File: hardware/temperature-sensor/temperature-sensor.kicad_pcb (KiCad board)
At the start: 2 copper layers, 56 x 56 mm, 3 parts, among them J1 1881626, U1 STM32F407V_E-G_Tx, U2 LAN8720A

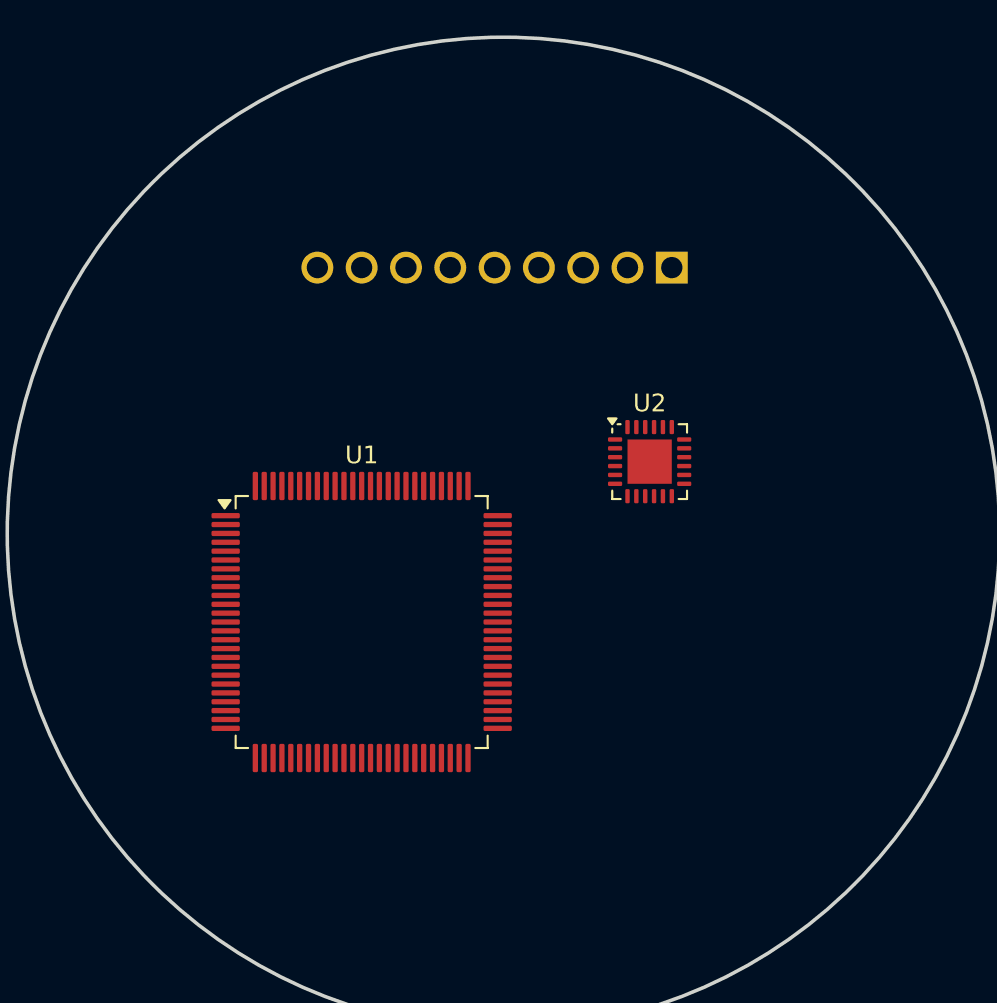
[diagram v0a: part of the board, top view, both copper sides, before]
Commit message: add components for temperature sensor
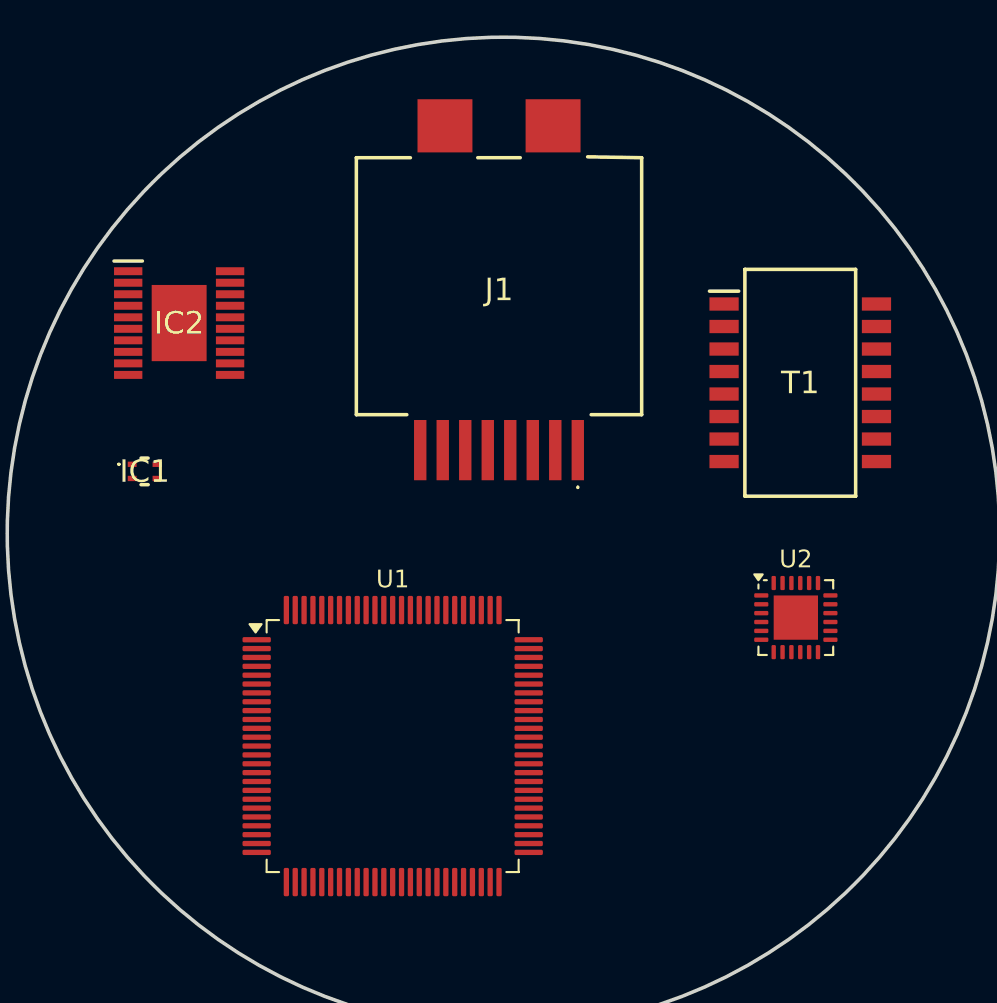
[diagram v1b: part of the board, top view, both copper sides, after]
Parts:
- added IC1: SHT40-CD1B-R3, benediktibk:SHT40CD1BR3, F.Cu at (129.8, 95.5)
- added IC2: PM8803TR, benediktibk:SOP65P640X120-21N, F.Cu at (131.7, 87.1)
- added T1: PT61018PEL, benediktibk:SOIC127P930X565-16N, F.Cu at (166.8, 90.5)
- J1: value 1881626 -> 1149611; footprint benediktibk:phoenix_contact_1881626 -> benediktibk:1149611; moved to F.Cu
- moved U2 12.1 mm to (166.5, 103.8)
- moved J1 9.83 mm to (149.8, 85.2), turned to 0 degrees
- moved U1 7.22 mm to (143.8, 111.0)

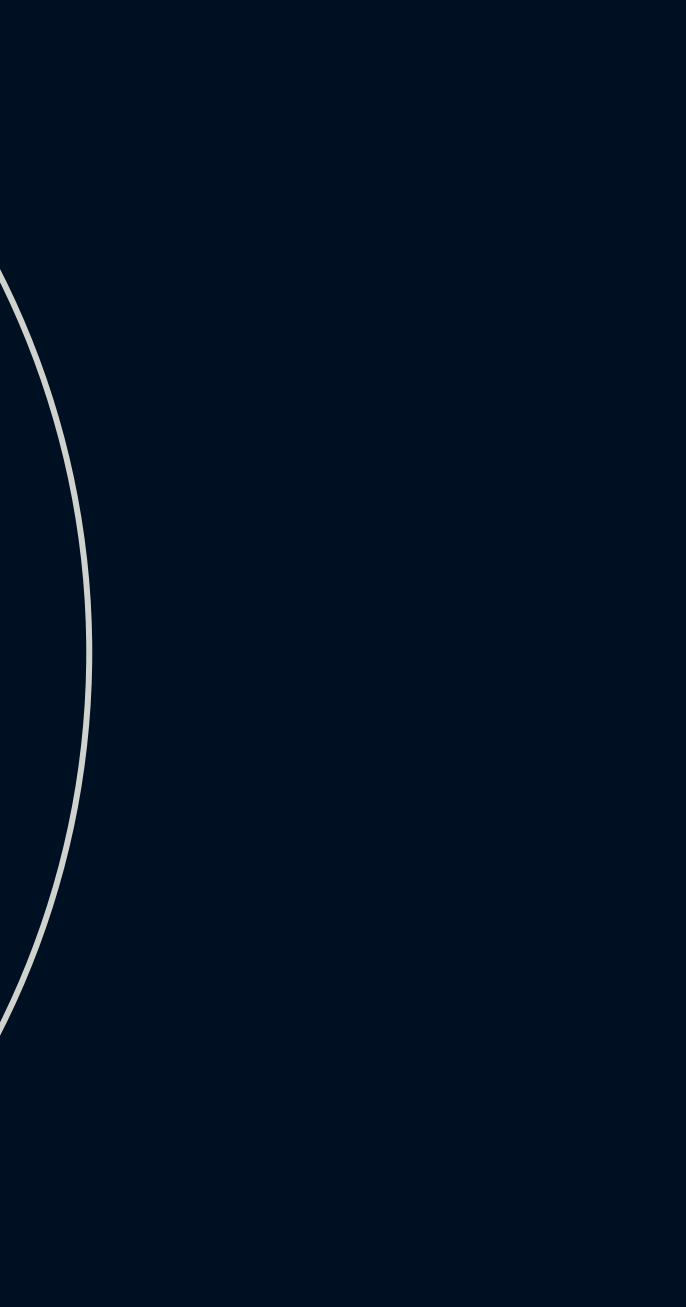
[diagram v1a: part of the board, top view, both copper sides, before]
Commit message: extend schematic of ethernet
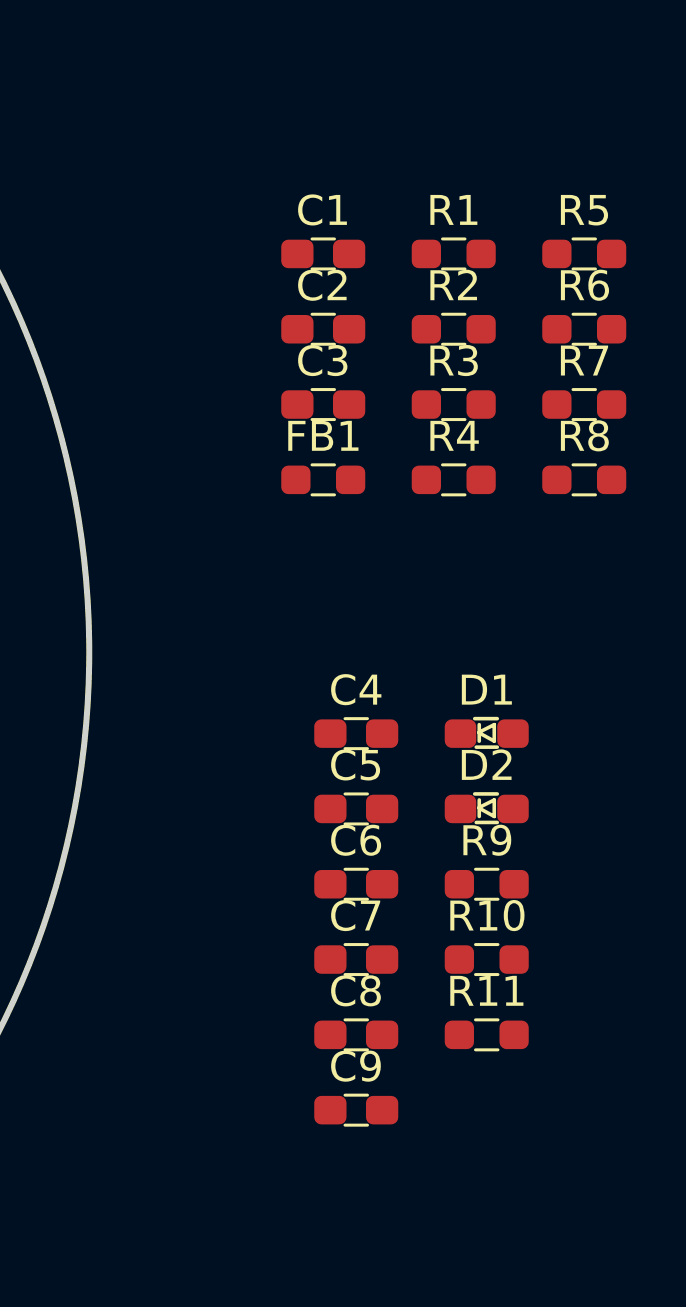
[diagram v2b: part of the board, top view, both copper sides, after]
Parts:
- added C1: 1nF 1kV, benediktibk:C_0603_1608Metric_Pad1.08x0.95mm_HandSolder, F.Cu at (185.8, 85.7)
- added C2: 100nF, benediktibk:C_0603_1608Metric_Pad1.08x0.95mm_HandSolder, F.Cu at (185.8, 88.2)
- added C3: 100nF, benediktibk:C_0603_1608Metric_Pad1.08x0.95mm_HandSolder, F.Cu at (185.8, 90.7)
- added C4: 100nF, benediktibk:C_0603_1608Metric_Pad1.08x0.95mm_HandSolder, F.Cu at (186.9, 101.7)
- added C5: 100nF, benediktibk:C_0603_1608Metric_Pad1.08x0.95mm_HandSolder, F.Cu at (186.9, 104.2)
- added C6: 100nF, benediktibk:C_0603_1608Metric_Pad1.08x0.95mm_HandSolder, F.Cu at (186.9, 106.7)
- added C7: 1uF, benediktibk:C_0603_1608Metric_Pad1.08x0.95mm_HandSolder, F.Cu at (186.9, 109.2)
- added C8: 1uF, benediktibk:C_0603_1608Metric_Pad1.08x0.95mm_HandSolder, F.Cu at (186.9, 111.8)
- added C9: 470pF, benediktibk:C_0603_1608Metric_Pad1.08x0.95mm_HandSolder, F.Cu at (186.9, 114.3)
- added D1: link/active, benediktibk:D_0603_1608Metric_Pad1.05x0.95mm_HandSolder, F.Cu at (191.2, 101.7)
- added D2: 100Mbps, benediktibk:D_0603_1608Metric_Pad1.05x0.95mm_HandSolder, F.Cu at (191.2, 104.2)
- added FB1: BLM18P, benediktibk:R_0603_1608Metric_Pad0.98x0.95mm_HandSolder, F.Cu at (185.8, 93.2)
- added R1: 75Ohm, benediktibk:R_0603_1608Metric_Pad0.98x0.95mm_HandSolder, F.Cu at (190.2, 85.7)
- added R10: 270Ohm, benediktibk:R_0603_1608Metric_Pad0.98x0.95mm_HandSolder, F.Cu at (191.2, 109.2)
- added R11: 12.1kOhm, benediktibk:R_0603_1608Metric_Pad0.98x0.95mm_HandSolder, F.Cu at (191.2, 111.8)
- added R2: 75Ohm, benediktibk:R_0603_1608Metric_Pad0.98x0.95mm_HandSolder, F.Cu at (190.2, 88.2)
- added R3: 75Ohm, benediktibk:R_0603_1608Metric_Pad0.98x0.95mm_HandSolder, F.Cu at (190.2, 90.7)
- added R4: 75Ohm, benediktibk:R_0603_1608Metric_Pad0.98x0.95mm_HandSolder, F.Cu at (190.2, 93.2)
- added R5: 47Ohm, benediktibk:R_0603_1608Metric_Pad0.98x0.95mm_HandSolder, F.Cu at (194.5, 85.7)
- added R6: 47Ohm, benediktibk:R_0603_1608Metric_Pad0.98x0.95mm_HandSolder, F.Cu at (194.5, 88.2)
- added R7: 47Ohm, benediktibk:R_0603_1608Metric_Pad0.98x0.95mm_HandSolder, F.Cu at (194.5, 90.7)
- added R8: 47Ohm, benediktibk:R_0603_1608Metric_Pad0.98x0.95mm_HandSolder, F.Cu at (194.5, 93.2)
- added R9: 270Ohm, benediktibk:R_0603_1608Metric_Pad0.98x0.95mm_HandSolder, F.Cu at (191.2, 106.7)
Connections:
- J1 pad 1: unconnected-(J1-Pad1) -> Net-(T1-TX+)
- J1 pad 2: unconnected-(J1-Pad2) -> Net-(T1-TX-)
- J1 pad 3: unconnected-(J1-Pad3) -> Net-(T1-RX+)
- J1 pad 4: unconnected-(J1-Pad4) -> Net-(J1-Pad4)
- J1 pad 5: unconnected-(J1-Pad5) -> Net-(J1-Pad4)
- J1 pad 6: unconnected-(J1-Pad6) -> Net-(T1-RX-)
- J1 pad 7: unconnected-(J1-Pad7) -> Net-(J1-Pad7)
- J1 pad 8: unconnected-(J1-Pad8) -> Net-(J1-Pad7)
- J1 pad MP1: unconnected-(J1-PadMP1) -> GND
- J1 pad MP2: unconnected-(J1-PadMP2) -> GND
- T1 pad 1: unconnected-(T1-TD+-Pad1) -> /Ethernet/TX_P
- T1 pad 10: unconnected-(T1-CT_3-Pad10) -> Net-(T1-CT_3)
- T1 pad 11: unconnected-(T1-RX+-Pad11) -> Net-(T1-RX+)
- T1 pad 14: unconnected-(T1-TX--Pad14) -> Net-(T1-TX-)
- T1 pad 15: unconnected-(T1-CT_4-Pad15) -> Net-(T1-CT_4)
- T1 pad 16: unconnected-(T1-TX+-Pad16) -> Net-(T1-TX+)
- T1 pad 2: unconnected-(T1-CT_1-Pad2) -> Net-(T1-CT_1)
- T1 pad 3: unconnected-(T1-TD--Pad3) -> /Ethernet/TX_N
- T1 pad 6: unconnected-(T1-RD+-Pad6) -> /Ethernet/RX_P
- T1 pad 7: unconnected-(T1-CT_2-Pad7) -> Net-(T1-CT_2)
- T1 pad 8: unconnected-(T1-RD--Pad8) -> /Ethernet/RX_N
- T1 pad 9: unconnected-(T1-RX--Pad9) -> Net-(T1-RX-)
- U2 pad 1: unconnected-(U2-VDD2A-Pad1) -> Net-(U2-VDD1A)
- U2 pad 10: unconnected-(U2-RXER/PHYAD0-Pad10) -> /Ethernet/RXER/PHYAD0
- U2 pad 11: unconnected-(U2-CRS_DV/MODE2-Pad11) -> /Ethernet/CRS_DV/MODE2
- U2 pad 12: unconnected-(U2-MDIO-Pad12) -> /Ethernet/MDIO
- U2 pad 13: unconnected-(U2-MDC-Pad13) -> /Ethernet/MDC
- U2 pad 14: unconnected-(U2-~{INT}/REFCLKO-Pad14) -> /Ethernet/REFCLK
- U2 pad 15: unconnected-(U2-~{RST}-Pad15) -> /Ethernet/nRST
- U2 pad 16: unconnected-(U2-TXEN-Pad16) -> /Ethernet/TXEN
- U2 pad 17: unconnected-(U2-TXD0-Pad17) -> /Ethernet/TXD0
- U2 pad 18: unconnected-(U2-TXD1-Pad18) -> /Ethernet/TXD1
- U2 pad 19: unconnected-(U2-VDD1A-Pad19) -> Net-(U2-VDD1A)
- U2 pad 2: unconnected-(U2-LED2/~{INTSEL}-Pad2) -> Net-(D2-A)
- U2 pad 20: unconnected-(U2-TXN-Pad20) -> /Ethernet/TX_N
- U2 pad 21: unconnected-(U2-TXP-Pad21) -> /Ethernet/TX_P
- U2 pad 22: unconnected-(U2-RXN-Pad22) -> /Ethernet/RX_N
- U2 pad 23: unconnected-(U2-RXP-Pad23) -> /Ethernet/RX_P
- U2 pad 24: unconnected-(U2-RBIAS-Pad24) -> Net-(U2-RBIAS)
- U2 pad 25: unconnected-(U2-VSS-Pad25) -> GND
- U2 pad 3: unconnected-(U2-LED1/REGOFF-Pad3) -> Net-(D1-A)
- U2 pad 6: unconnected-(U2-VDDCR-Pad6) -> Net-(U2-VDDCR)
- U2 pad 7: unconnected-(U2-RXD1/MODE1-Pad7) -> /Ethernet/RXD1/MODE1
- U2 pad 8: unconnected-(U2-RXD0/MODE0-Pad8) -> /Ethernet/RXD0/MODE0
- U2 pad 9: unconnected-(U2-VDDIO-Pad9) -> Net-(U2-VDD1A)

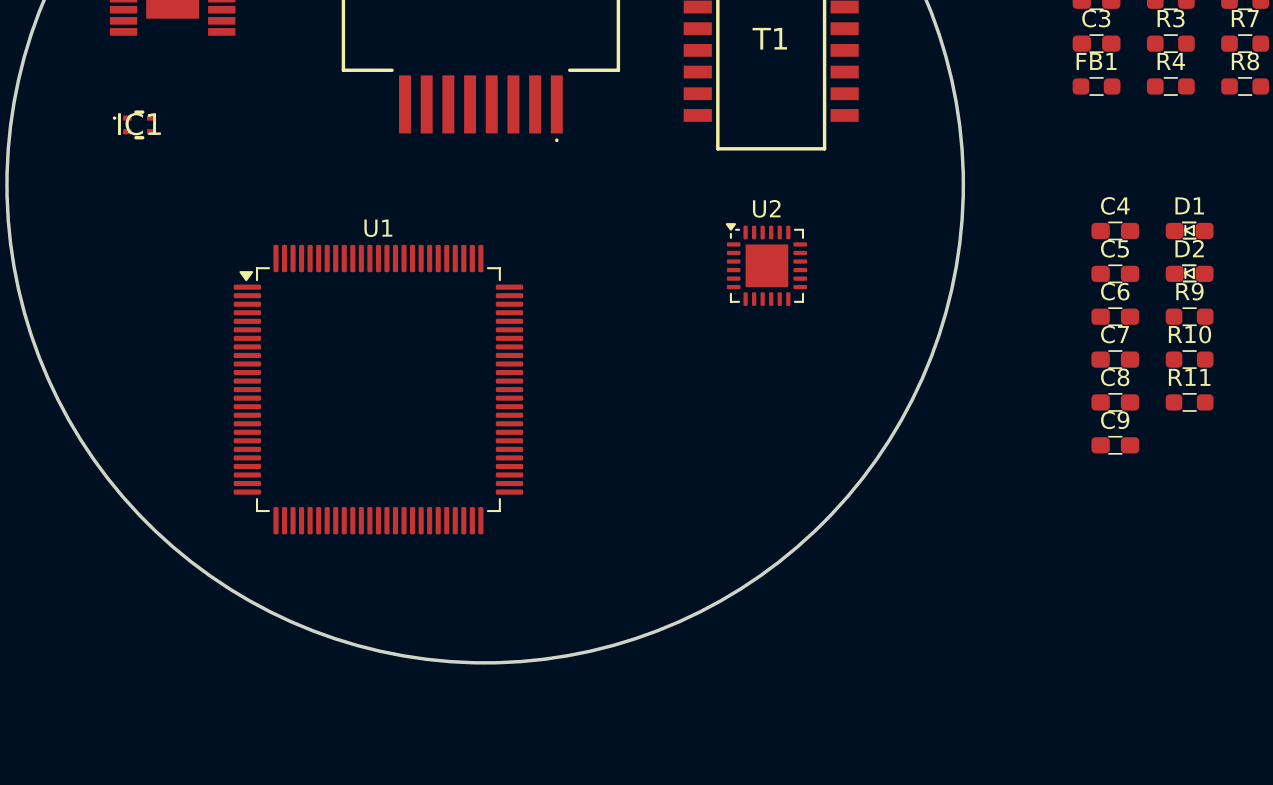
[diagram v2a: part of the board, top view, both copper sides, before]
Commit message: add quartz
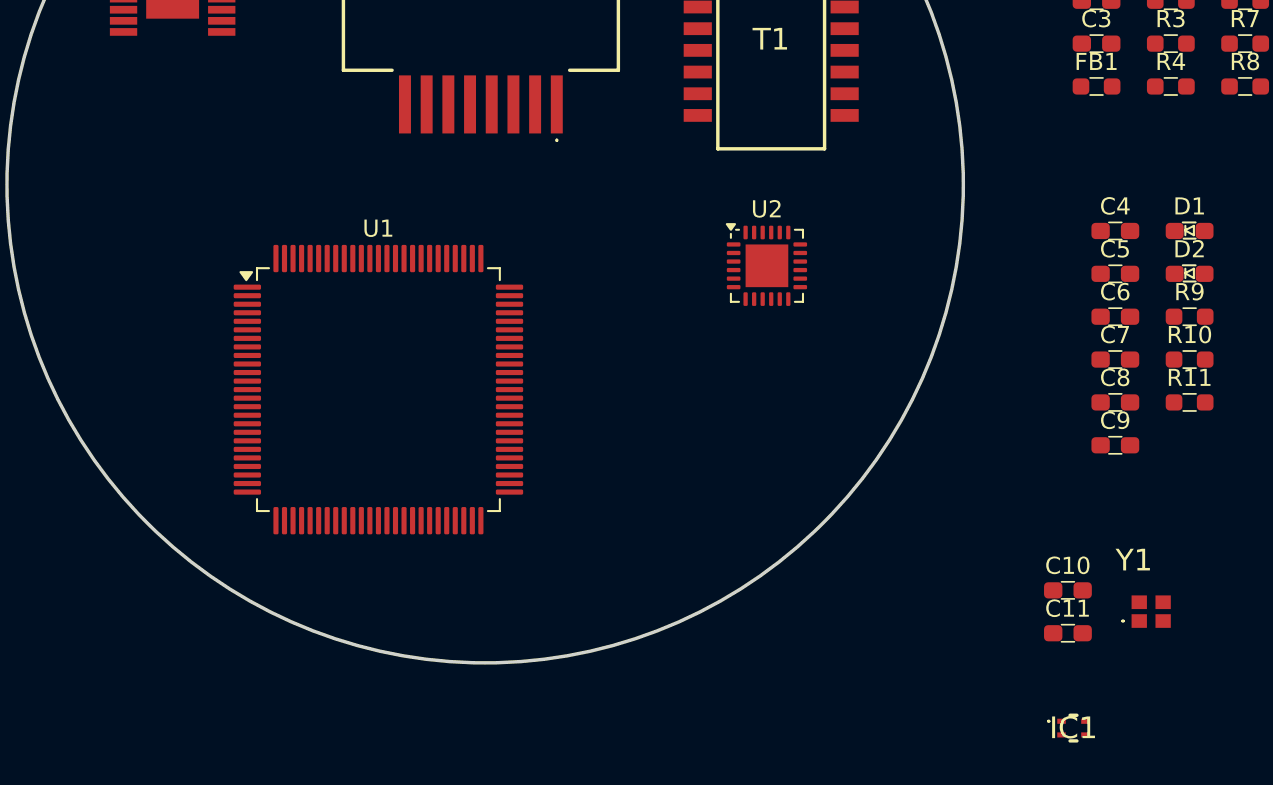
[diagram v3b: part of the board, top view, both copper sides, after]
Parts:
- added C10: 3.5pF, benediktibk:C_0603_1608Metric_Pad1.08x0.95mm_HandSolder, F.Cu at (184.1, 122.8)
- added C11: 3.5pF, benediktibk:C_0603_1608Metric_Pad1.08x0.95mm_HandSolder, F.Cu at (184.1, 125.3)
- added Y1: CX2016FB25000C0FZZH1, benediktibk:CX2016FB25000C0FZZH1, F.Cu at (189.0, 124.0)
- moved IC1 65.1 mm to (184.4, 130.8)
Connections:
- U1 pad 12: unconnected-(U1-PH0-Pad12) -> Net-(U1-PH0)
- U1 pad 13: unconnected-(U1-PH1-Pad13) -> Net-(U1-PH1)
- U2 pad 5: unconnected-(U2-XTAL1/CLKIN-Pad5) -> /Ethernet/CLK
